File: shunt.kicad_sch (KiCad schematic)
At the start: 39 parts, among them J1 Screw_Terminal_01x03, U2 INA219AxD

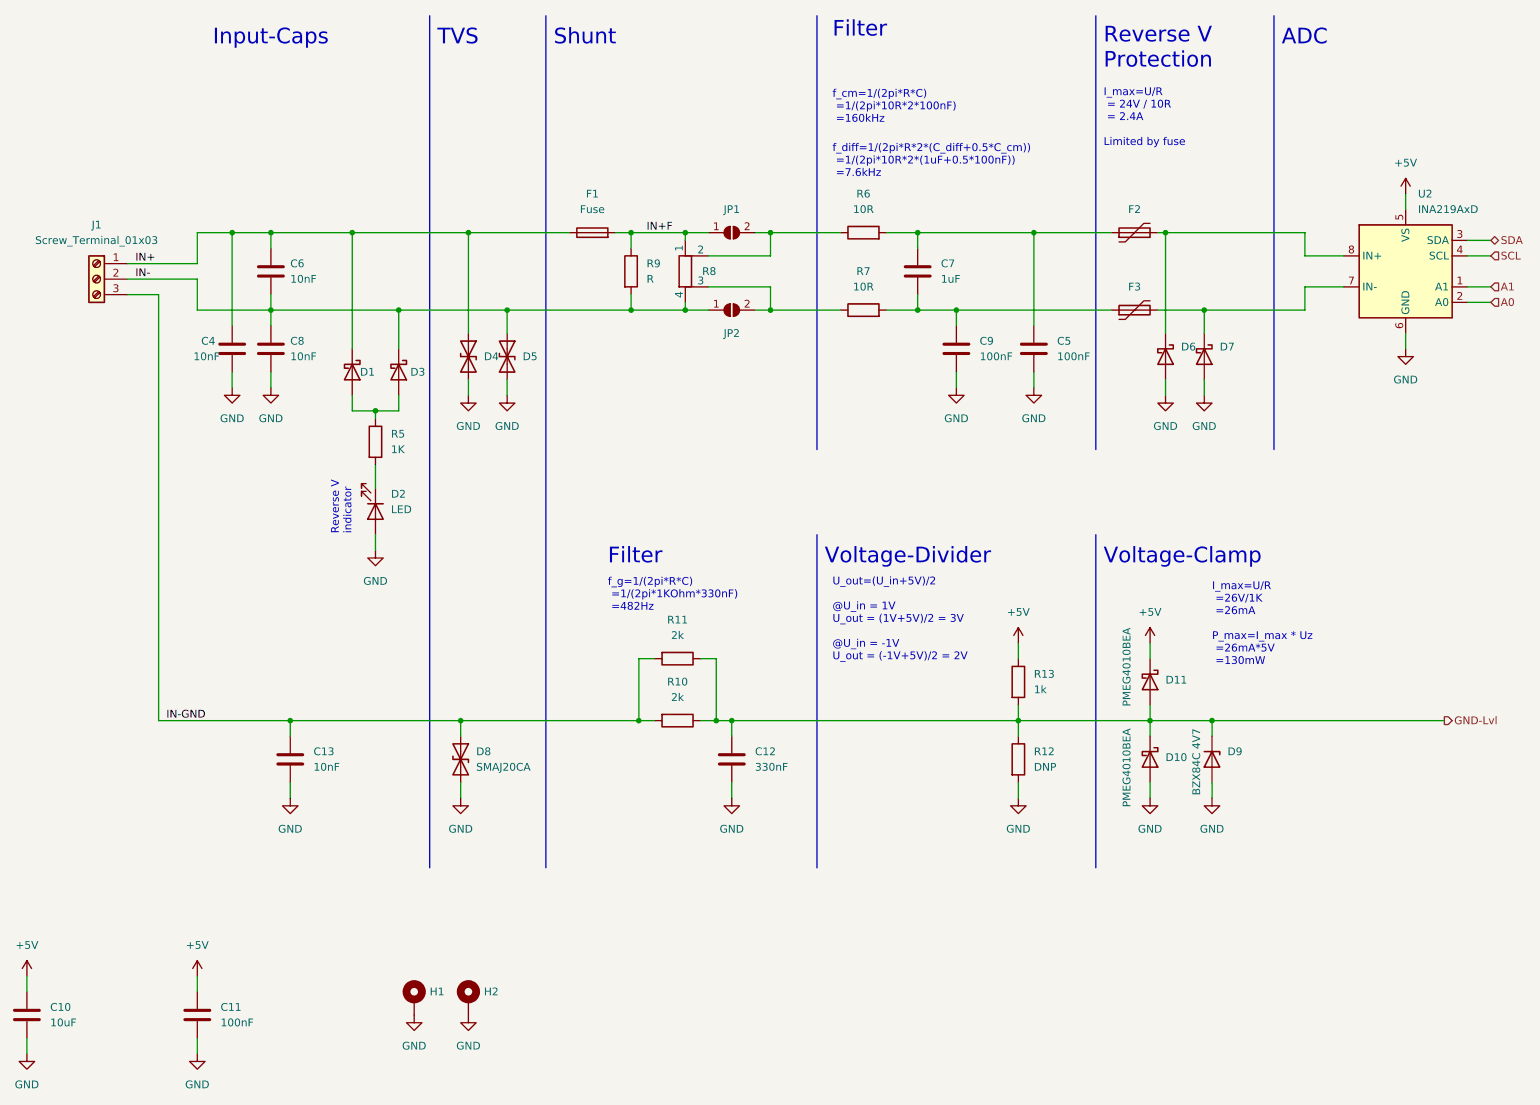
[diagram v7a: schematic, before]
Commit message: Shrink board and reduce features to reduce price
* Shrink to 100mm x 50mm
* Remove voltage regulator and use Stemma Power instead
* Remove isolation (is easier to add outside when needed)
* Remove reverse indicators to save space
* Remove I2C pullups as they are no longer needed
* Fix A2 of EEPROM and Temperature sensor to 0 to save space
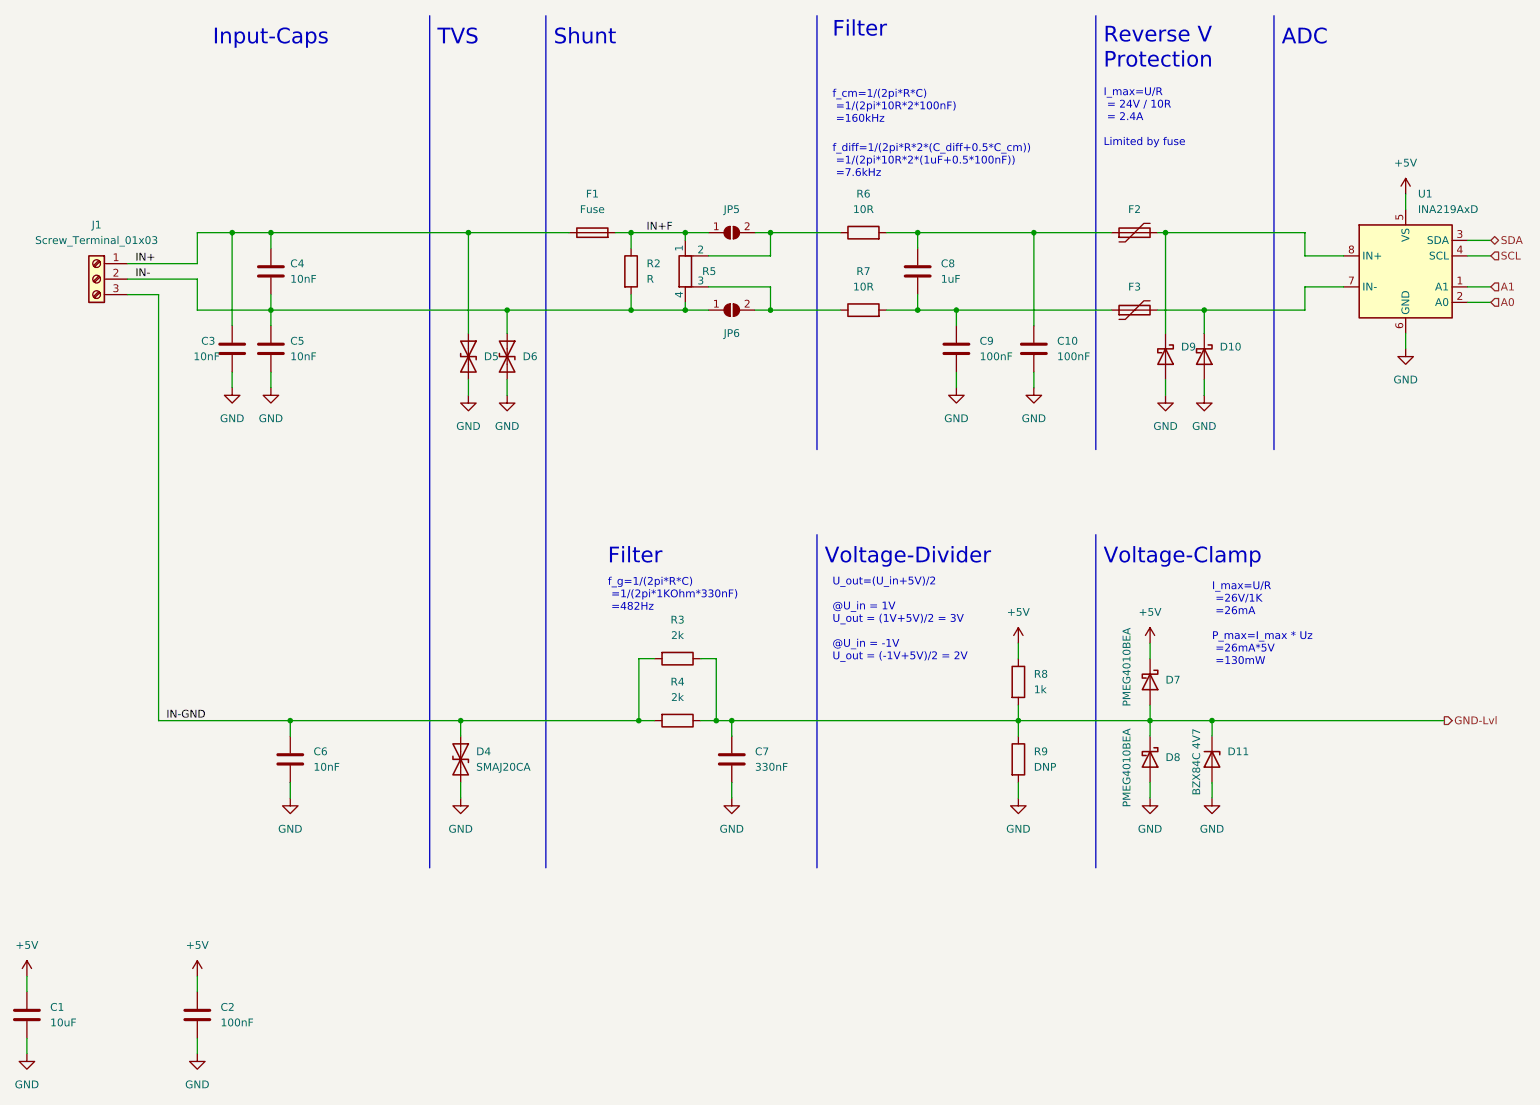
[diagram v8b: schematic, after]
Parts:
- removed D1, D3: PMEG4010BEA, Diode_SMD:D_SOD-323F, symbol Device:D_Schottky
- removed D2: LED, LED_SMD:LED_0603_1608Metric, symbol Device:LED
- removed H1, H2: MountingHole_Pad, MountingHole:MountingHole_3.2mm_M3_Pad_Via, symbol Mechanical:MountingHole_Pad
- removed R5: 1K, Resistor_SMD:R_0603_1608Metric, symbol Device:R
- renumbered C10 to C1, C5 to C10, C11 to C2, C4 to C3, C6 to C4, C8 to C5, C13 to C6, C12 to C7, C7 to C8, D7 to D10, D9 to D11, D8 to D4, D4 to D5, D5 to D6, D11 to D7, D10 to D8, D6 to D9, JP1 to JP5, JP2 to JP6, R9 to R2, R11 to R3, R10 to R4, R8 to R5, R13 to R8, R12 to R9, U2 to U1
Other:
- note removed: "Reverse V indicator"
